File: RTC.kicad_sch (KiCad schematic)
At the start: 5 parts, among them U501 DS3231M+TRL

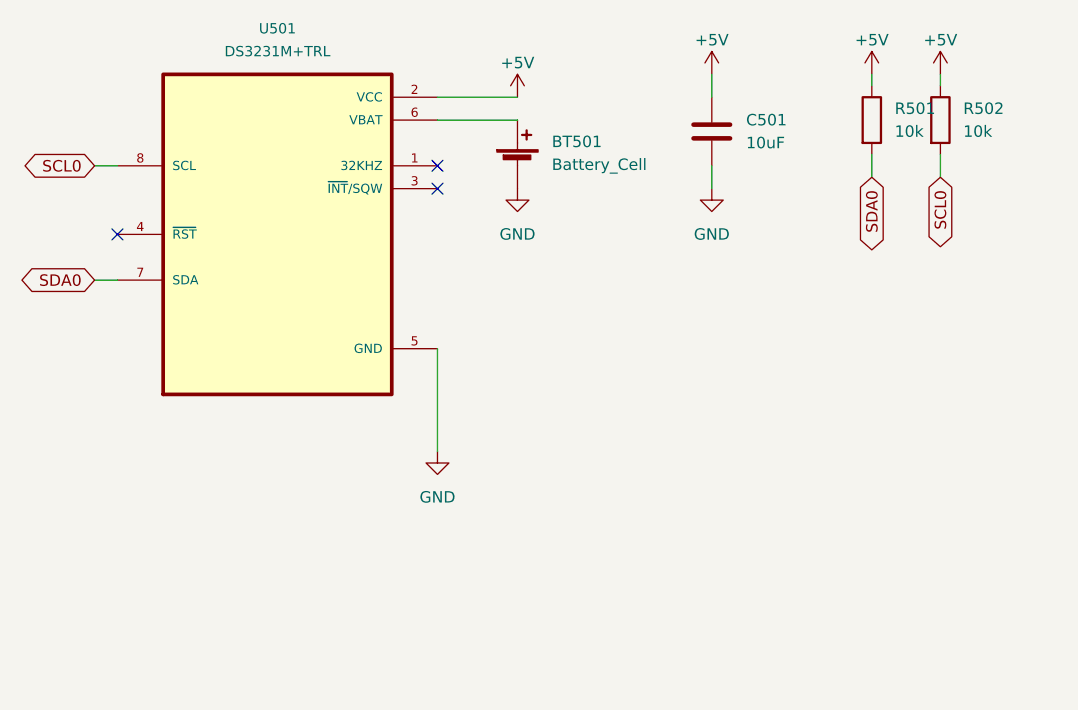
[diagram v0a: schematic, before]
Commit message: CM4>RP3/4
changed SBC to RP3/4
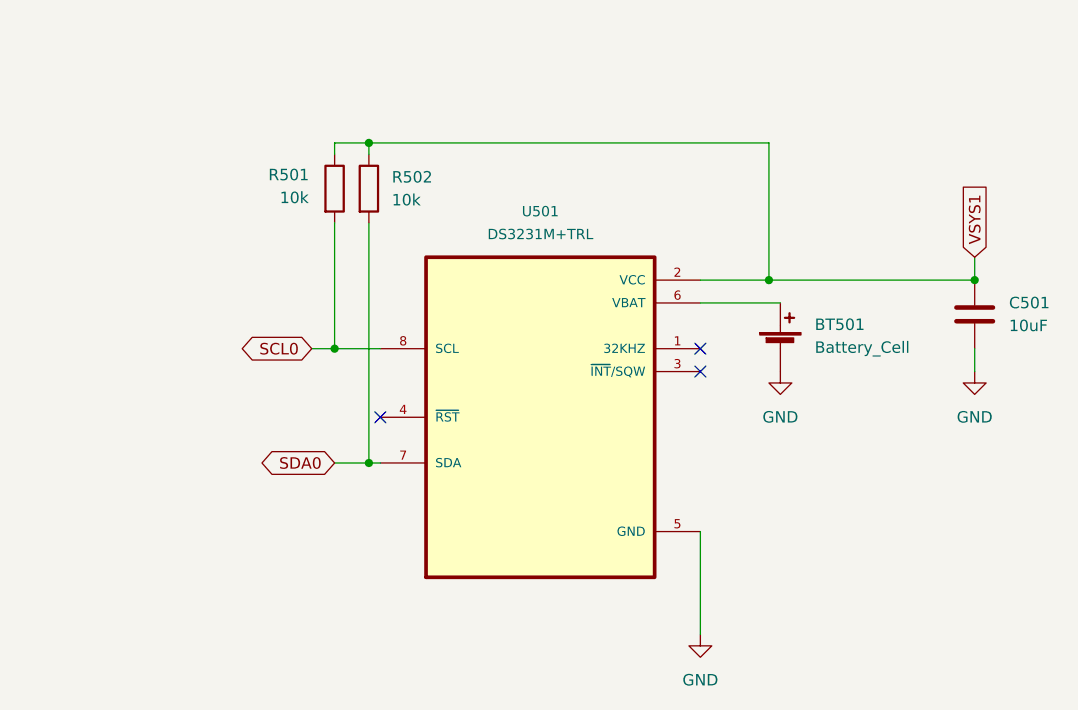
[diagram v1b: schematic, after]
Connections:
- net SCL0: now also R501.2; no longer R502.2
- net SDA0: now also R502.2; no longer R501.2
- net +5V renamed VSYS1
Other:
- moved on the sheet: BT501, C501, R501, R502, U501
